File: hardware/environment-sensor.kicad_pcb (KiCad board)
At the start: 2 copper layers, 111 x 86 mm, 108 parts, among them P2 ICSP, P4 JTAG, P5 RB1-125BAG1A, P6 NSL-19M51, P7 PPD42, P8 POWER, SW1 Reset, U1 ATMEGA32U4-AU, U2 W5500, U3 Bosch_BME280, U4 LM317T, U5 LM317T, X1 16MHz, X2 25MHz

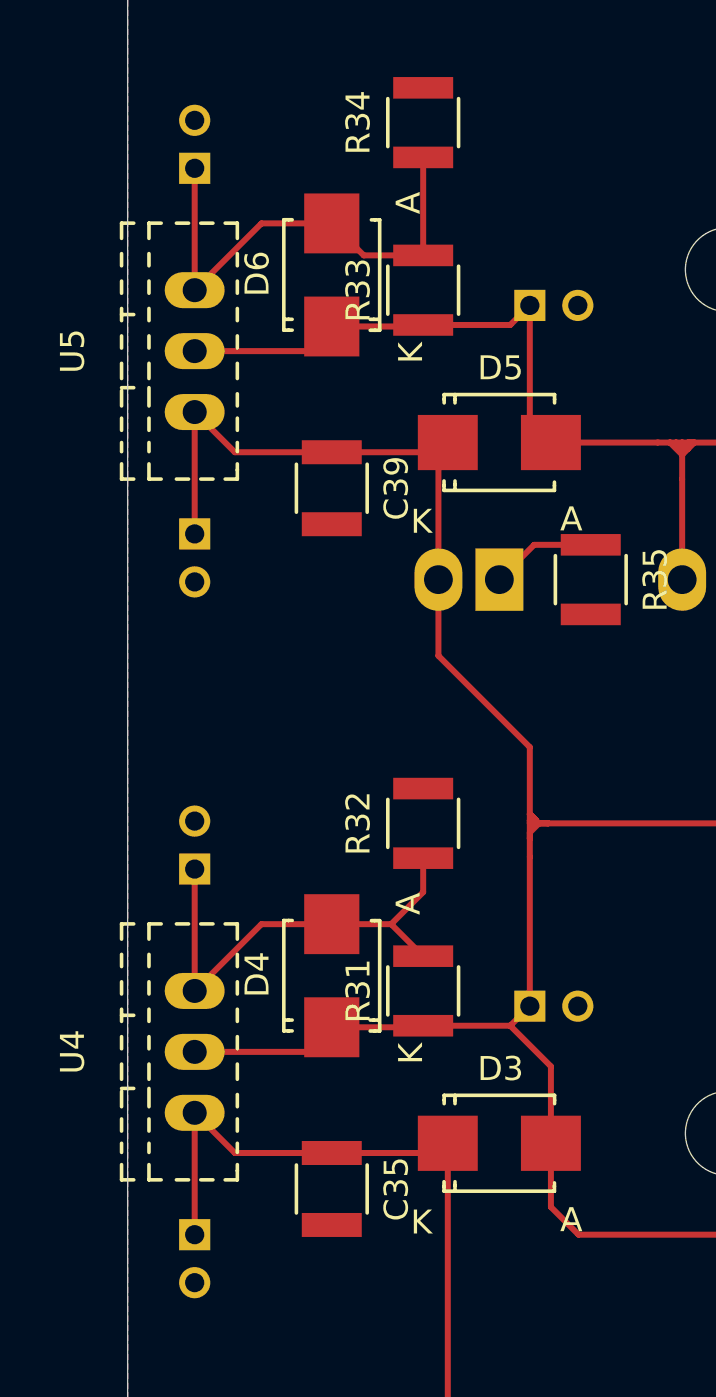
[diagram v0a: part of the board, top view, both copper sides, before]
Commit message: Add planes for regulators
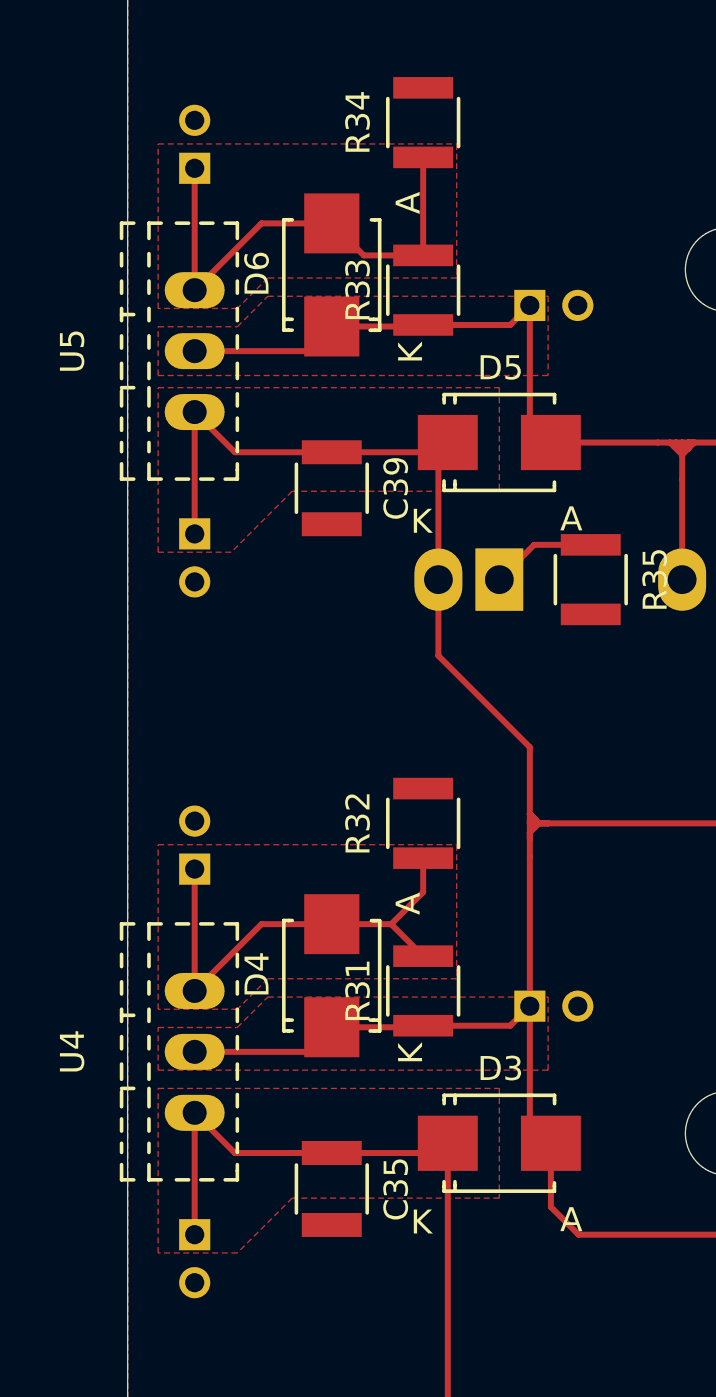
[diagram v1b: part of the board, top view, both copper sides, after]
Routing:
- added copper zone on F.Cu, net /Microcontroller/3V3A
- added copper zone on F.Cu, net /Power Supply/+6V
- added copper zone on F.Cu, net /Power Supply/5VA
- added copper zone on F.Cu, net Net-(C36-Pad1)
- added copper zone on F.Cu, net Net-(C40-Pad1)
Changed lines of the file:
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@@
   (layers
     (0 F.Cu signal)
-    (31 B.Cu signal)
+    (31 B.Cu signal hide)
     (32 B.Adhes user)
     (33 F.Adhes user)
@@
     (last_trace_width 0.25)
     (trace_clearance 0.2)
-    (zone_clearance 0.2)
-    (zone_45_only no)
+    (zone_clearance 0.3)
+    (zone_45_only yes)
     (trace_min 0.2)
     (segment_width 0.2)
@@
   (segment (start 159.004 100.076) (end 159.004 99.822) (width 0.25) (layer B.Cu) (net 16))
   (segment (start 159.586 106.172) (end 159.586 103.124) (width 0.25) (layer B.Cu) (net 16))
+  (segment (start 118.98884 119.38) (end 118.11 118.50116) (width 0.25) (layer F.Cu) (net 17) (status C00000))
+  (segment (start 118.11 118.50116) (end 118.11 113.665) (width 0.25) (layer F.Cu) (net 17) (status C00000))
   (segment (start 104.14 93.98) (end 104.14 88.9) (width 0.25) (layer F.Cu) (net 17))
   (segment (start 109.855 90.575) (end 105.815 90.575) (width 0.25) (layer F.Cu) (net 17))
@@
   (segment (start 118.98884 122.03684) (end 118.98884 119.38) (width 0.25) (layer F.Cu) (net 17))
   (segment (start 120.142 123.19) (end 118.98884 122.03684) (width 0.25) (layer F.Cu) (net 17))
-  (segment (start 117.295 114.48) (end 118.98884 116.17384) (width 0.25) (layer F.Cu) (net 17))
-  (segment (start 118.98884 116.17384) (end 118.98884 119.38) (width 0.25) (layer F.Cu) (net 17))
   (segment (start 113.665 114.48) (end 117.295 114.48) (width 0.25) (layer F.Cu) (net 17))
   (segment (start 117.295 114.48) (end 118.11 113.665) (width 0.25) (layer F.Cu) (net 17))
@@
       )
     )
+  )
+  (zone (net 17) (net_name "/Power Supply/5VA") (layer F.Cu) (hatch edge 0.508)
+    (priority 1)
+    (connect_pads (clearance 0.3))
+    (min_thickness 0.254)
+    (fill (arc_segments 32) (thermal_gap 0.508) (thermal_bridge_width 0.508))
+    (polygon
+      (pts
+        (xy 116.84 92.202) (xy 108.204 92.202) (xy 105.664 94.742) (xy 102.616 94.742) (xy 102.616 87.884)
+        (xy 116.84 87.884)
+      )
+    )
+  )
+  (zone (net 7) (net_name /Microcontroller/3V3A) (layer F.Cu) (hatch edge 0.508)
+    (priority 1)
+    (connect_pads (clearance 0.3))
+    (min_thickness 0.254)
+    (fill (arc_segments 32) (thermal_gap 0.508) (thermal_bridge_width 0.508))
+    (polygon
+      (pts
+        (xy 118.872 87.376) (xy 102.616 87.376) (xy 102.616 85.344) (xy 105.918 85.344) (xy 107.188 84.074)
+        (xy 118.872 84.074)
+      )
+    )
+  )
+  (zone (net 20) (net_name "Net-(C40-Pad1)") (layer F.Cu) (hatch edge 0.508)
+    (priority 1)
+    (connect_pads (clearance 0.3))
+    (min_thickness 0.254)
+    (fill (arc_segments 32) (thermal_gap 0.508) (thermal_bridge_width 0.508))
+    (polygon
+      (pts
+        (xy 115.062 83.312) (xy 107.188 83.312) (xy 105.918 84.582) (xy 102.616 84.582) (xy 102.616 77.724)
+        (xy 115.062 77.724)
+      )
+    )
+  )
+  (zone (net 18) (net_name "/Power Supply/+6V") (layer F.Cu) (hatch edge 0.508)
+    (priority 1)
+    (connect_pads (clearance 0.3))
+    (min_thickness 0.254)
+    (fill (arc_segments 32) (thermal_gap 0.508) (thermal_bridge_width 0.508))
+    (polygon
+      (pts
+        (xy 116.84 121.666) (xy 108.204 121.666) (xy 105.918 123.952) (xy 102.616 123.952) (xy 102.616 117.094)
+        (xy 116.84 117.094)
+      )
+    )
+  )
+  (zone (net 17) (net_name "/Power Supply/5VA") (layer F.Cu) (hatch edge 0.508)
+    (priority 1)
+    (connect_pads (clearance 0.3))
+    (min_thickness 0.254)
+    (fill (arc_segments 32) (thermal_gap 0.508) (thermal_bridge_width 0.508))
+    (polygon
+      (pts
+        (xy 118.872 116.332) (xy 102.616 116.332) (xy 102.616 114.554) (xy 105.918 114.554) (xy 107.188 113.284)
+        (xy 118.872 113.284)
+      )
+    )
+  )
+  (zone (net 19) (net_name "Net-(C36-Pad1)") (layer F.Cu) (hatch edge 0.508)
+    (priority 1)
+    (connect_pads (clearance 0.3))
+    (min_thickness 0.254)
+    (fill (arc_segments 32) (thermal_gap 0.508) (thermal_bridge_width 0.508))
+    (polygon
+      (pts
+        (xy 115.062 112.522) (xy 107.188 112.522) (xy 105.918 113.792) (xy 102.616 113.792) (xy 102.616 106.934)
+        (xy 115.062 106.934)
+      )
+    )

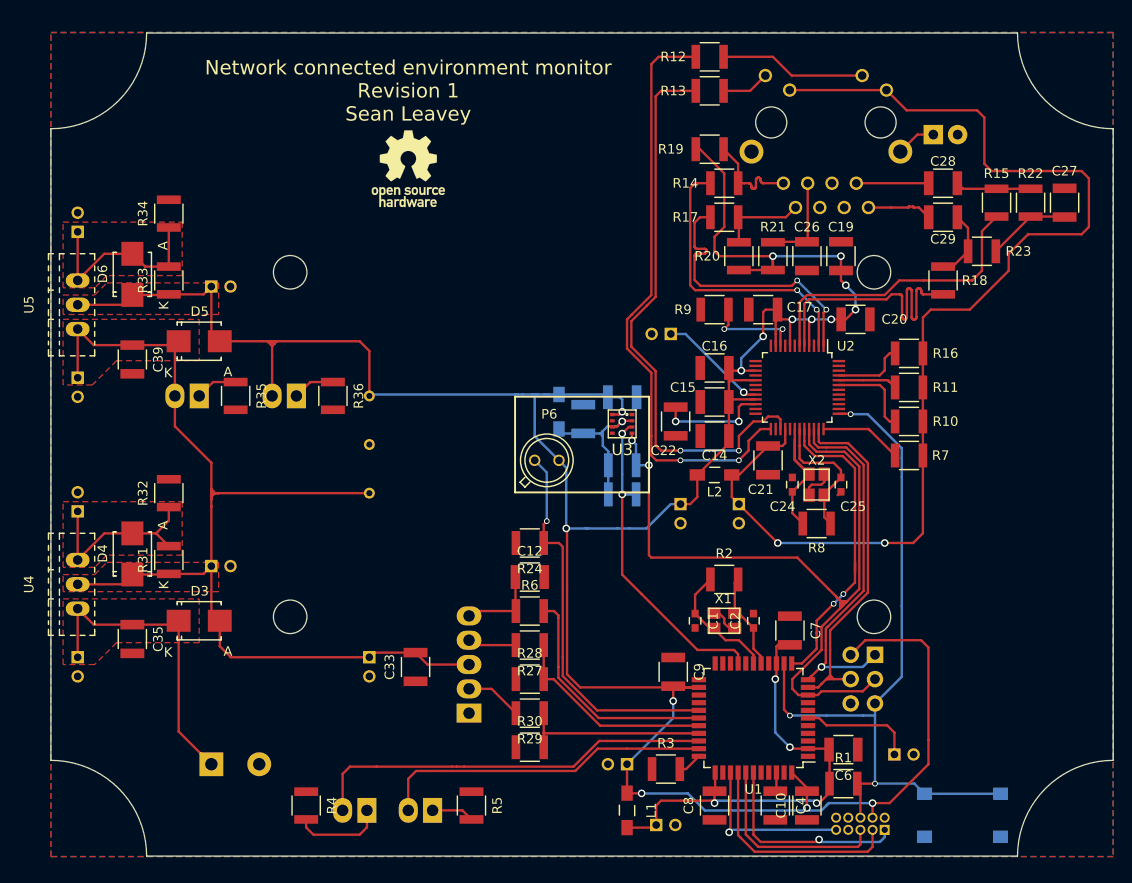
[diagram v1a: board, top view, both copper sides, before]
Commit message: Move labels, replace some SMB diodes with SMA, final tweaks
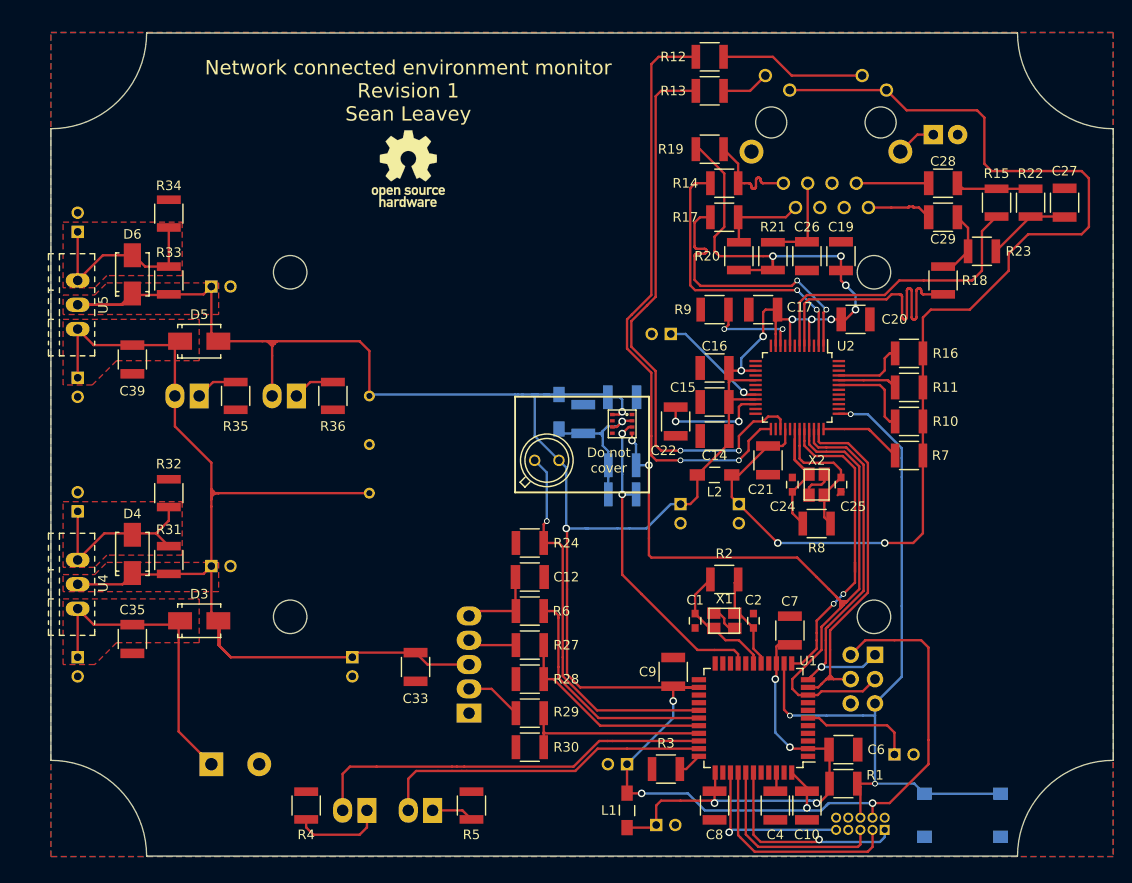
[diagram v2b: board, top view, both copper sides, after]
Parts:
- D3, D4, D5, D6: value S1KB-13-F -> S1B-13-F; footprint Diodes_SMD:SMB_Standard -> Diodes_SMD:SMA_Standard
- moved C32 1.78 mm to (132.8, 123.2)
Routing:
- net /Microcontroller/3V3A: track 309.2 -> 315.4 mm
- net /Power Supply/5VA: track 111.7 -> 116.0 mm
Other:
- board text added: "+6V"
- board text added: "3.3V"
- board text added: "5V"
- board text added: "Black"
- board text added: "Do not cover"
- board text added: "GND"
- board text added: "Green"
- board text added: "ICSP"
- board text added: "JTAG"
- board text added: "PPD42"
- board text added: "RJ45 shield ground"
- board text added: "Red"
- board text added: "Reset"
- board text added: "White"
- board text added: "Yellow"

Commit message: Move LM317 regulator footprints to underside; final tweaks
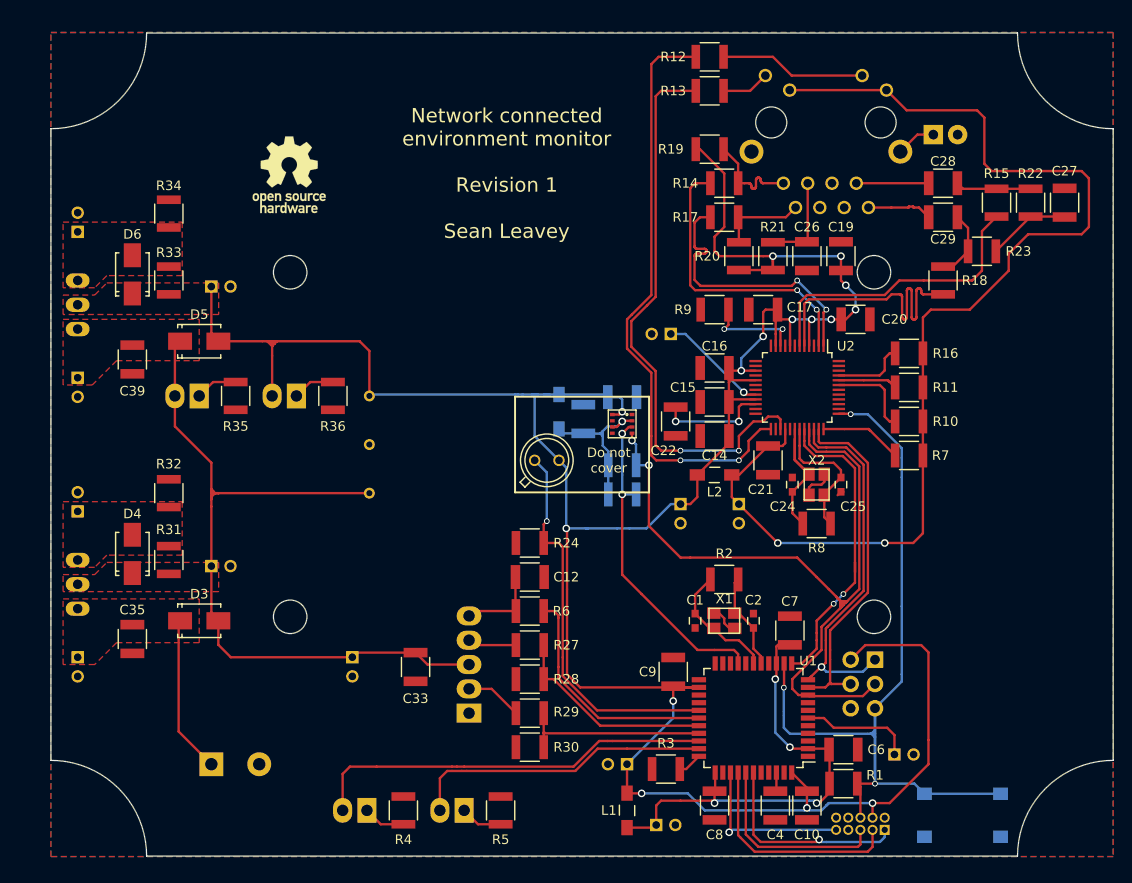
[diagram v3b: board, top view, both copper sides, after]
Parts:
- added REF***: OSHW-Logo_7.5x8mm_SilkScreen, Symbols:OSHW-Logo_7.5x8mm_SilkScreen, B.Cu at (126.2, 72.8)
- U4, U5: footprint TO_SOT_Packages_THT:TO-220_Neutral123_Vertical_MountedFromLS -> TO_SOT_Packages_THT:TO-220_Neutral123_Vertical; moved to B.Cu
- moved REF*** 12.5 mm to (126.2, 72.8)
- moved R4 10.2 mm to (138.2, 139.2)
- moved D2 3.30 mm to (144.5, 139.2)
- moved R5 3.09 mm to (148.3, 139.2)
- moved P2 0.51 mm to (187.5, 123.4)
- turned U4 to 270 degrees
- turned U5 to 270 degrees
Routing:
- net /Power Supply/5VA: track 116.0 -> 81.1 mm
- net /Microcontroller/3V3A: track 315.4 -> 294.1 mm
- net Net-(C40-Pad1): track 20.3 -> 0.00 mm
- net Net-(C36-Pad1): track 19.6 -> 0.00 mm
- net /Power Supply/+6V: track 32.9 -> 17.0 mm
- net /Microcontroller/~RESET: track 78.0 -> 88.3 mm
- net Net-(D1-Pad1): track 9.60 -> 4.41 mm
- net Net-(D2-Pad2): track 35.0 -> 31.7 mm
- net /Microcontroller/SCLK: track 84.2 -> 82.3 mm
- net /Microcontroller/MOSI: track 37.5 -> 37.0 mm
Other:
- board text added: "1"
- board text added: "3.3V On"
- board text added: "5V On"
- board text added: "Status 1"
- board text added: "Status 2"
